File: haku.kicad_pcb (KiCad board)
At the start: 2 copper layers, 323.9 x 97 mm, 172 parts, among them SW1 SW_Push, U1 ATmega32U4-AU, U2 SRV05-4, Y1 16MHz

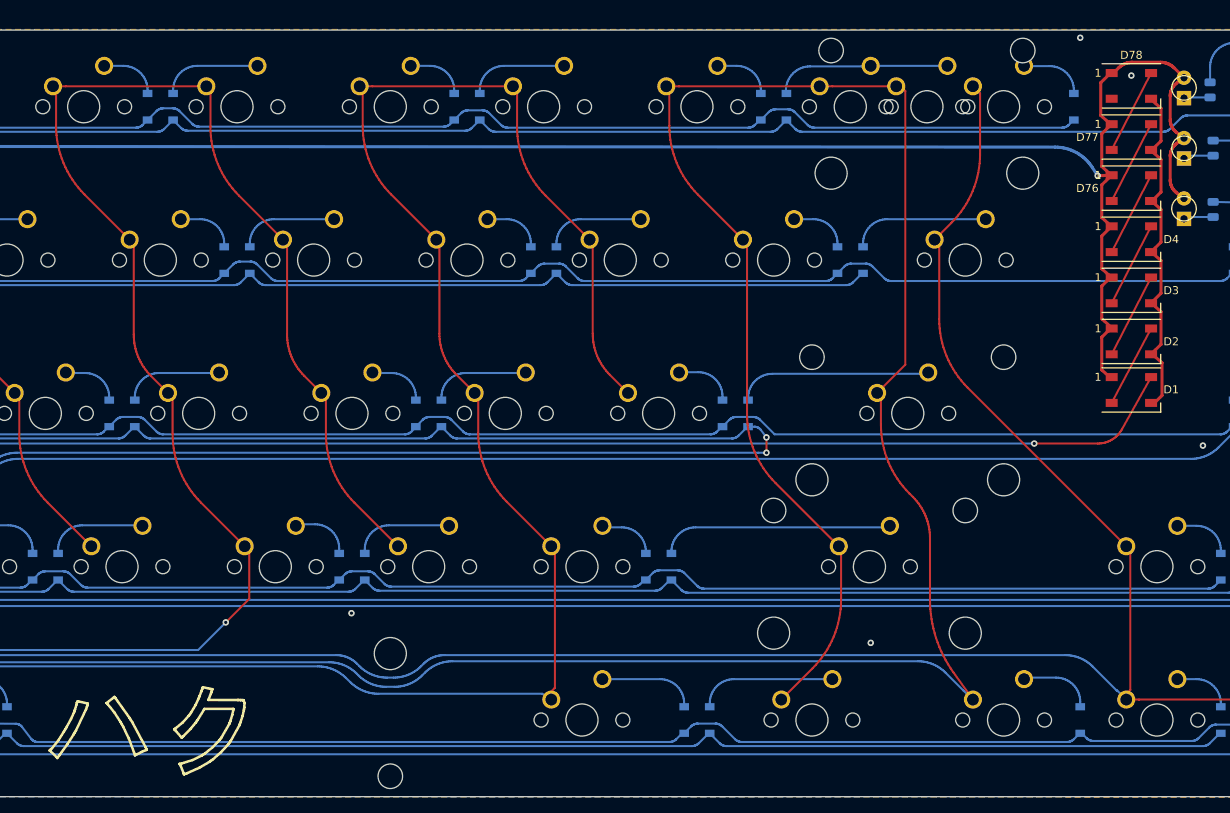
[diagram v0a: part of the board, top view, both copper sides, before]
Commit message: remove silkscreen artwork, add exposed soldermask artwork
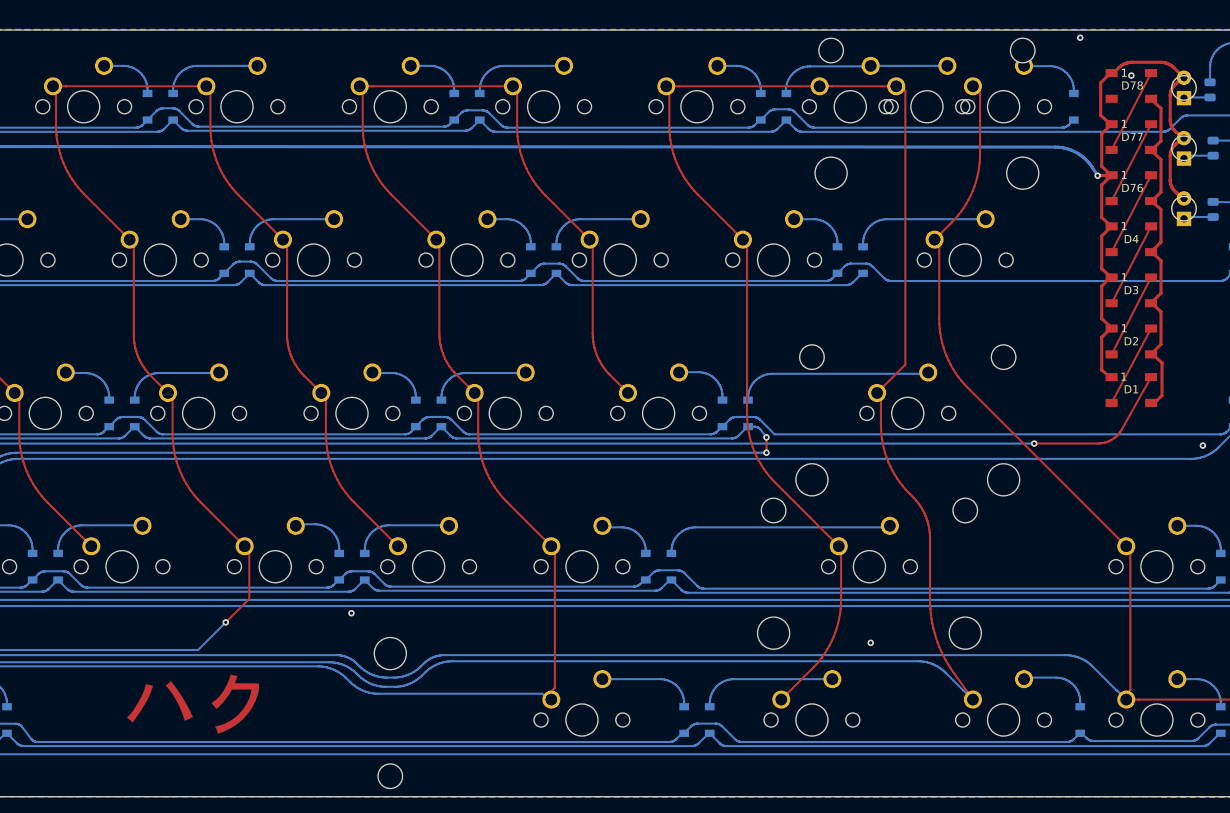
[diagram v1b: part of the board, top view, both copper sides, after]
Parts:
- added G***: LOGO, board_logos:haku, F.Cu at (223.1, 171.1)

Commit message: move components, update traces
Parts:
- R4, R5: value 10k -> 22
- moved R5 60.9 mm to (143.2, 175.1), turned to 135 degrees
- moved R4 59.1 mm to (144.9, 173.5), turned to 135 degrees
- moved C4 6.42 mm to (149.4, 175.3), turned to 180 degrees
- moved C8 5.26 mm to (149.4, 178.4), turned to 180 degrees
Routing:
- net D-: track 37.8 -> 106.1 mm
- net D+: track 39.4 -> 107.3 mm
- net /D1-: track 80.2 -> 12.7 mm
- net /D1+: track 79.2 -> 12.1 mm
- net +5V: track 510.2 -> 498.6 mm, vias 15 -> 11
- net Net-(C8-Pad1): track 11.1 -> 6.67 mm
- net Row9: track 280.3 -> 282.1 mm
- net Row8: track 309.6 -> 311.4 mm
- net Col4: track 227.9 -> 227.4 mm
- net GND: track 149.6 -> 149.9 mm, vias 16 -> 18

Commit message: designed by illusion
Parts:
- added G***: LOGO, board_logos:designed-by2, F.Cu at (52.7, 180.0)
- moved R5 3.07 mm to (144.2, 178.0), turned to 180 degrees
- moved R4 2.31 mm to (144.2, 175.7), turned to 180 degrees
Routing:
- net GND: track 149.9 -> 146.0 mm
- net D-: track 106.1 -> 107.5 mm
- net /D1-: track 12.7 -> 11.3 mm
- net D+: track 107.3 -> 108.4 mm
- net /D1+: track 12.1 -> 11.1 mm
- net Row7: track 349.4 -> 348.7 mm

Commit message: lots of changes
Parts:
- added C10: 0.1uF, Capacitor_SMD:C_0805_2012Metric, B.Cu at (335.9, 103.9)
- added C11: 0.1uF, Capacitor_SMD:C_0805_2012Metric, B.Cu at (335.9, 110.1)
- added C12: 0.1uF, Capacitor_SMD:C_0805_2012Metric, B.Cu at (335.9, 116.5)
- added C13: 0.1uF, Capacitor_SMD:C_0805_2012Metric, B.Cu at (335.9, 122.8)
- added C14: 0.1uF, Capacitor_SMD:C_0805_2012Metric, B.Cu at (335.8, 129.0)
- added C9: 0.1uF, Capacitor_SMD:C_0805_2012Metric, B.Cu at (335.7, 96.5)
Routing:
- net +5V: track 498.6 -> 513.0 mm, vias 11 -> 21
